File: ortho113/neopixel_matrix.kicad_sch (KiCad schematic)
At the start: 113 parts

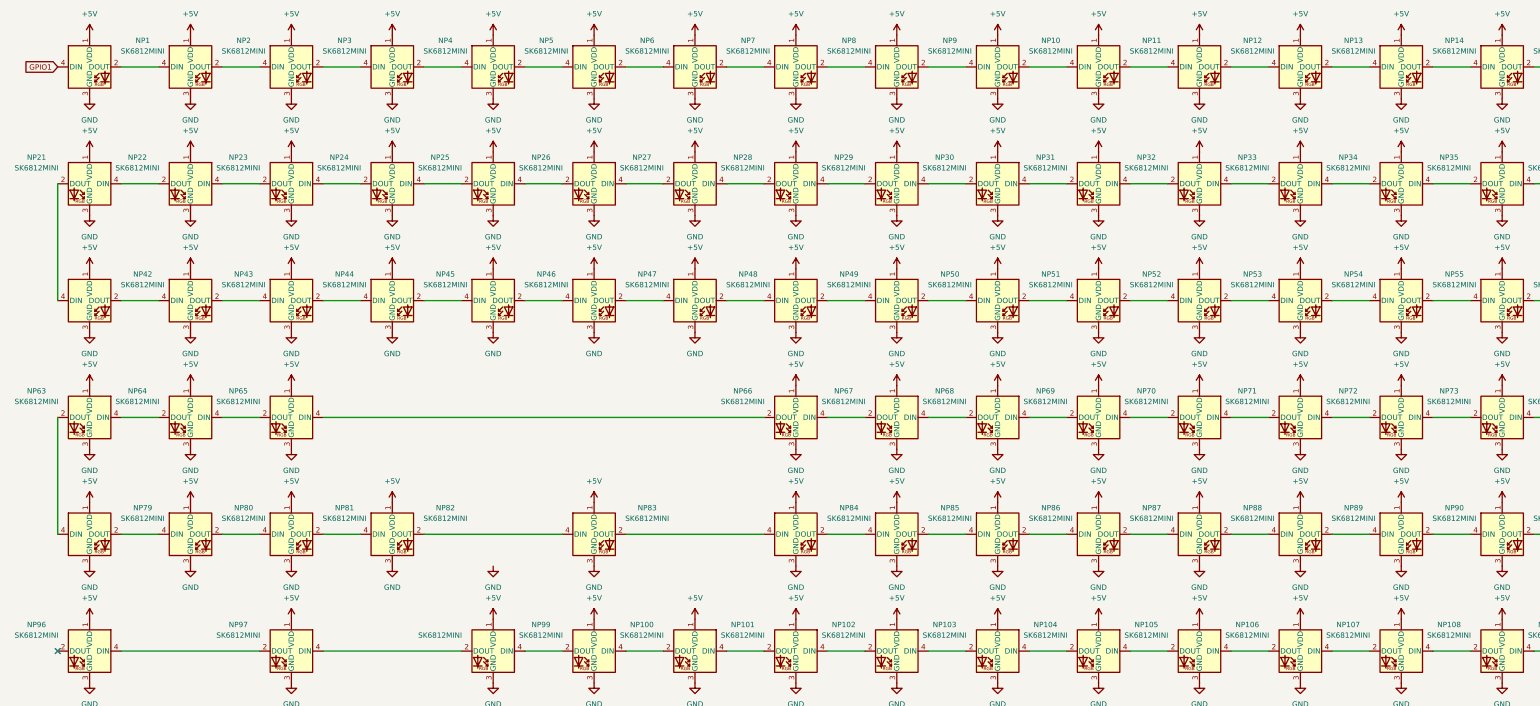
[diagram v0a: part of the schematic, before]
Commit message: fixed submodule conflict & remove gitignore
added pinout for oled display
finished rev1 of pcb design
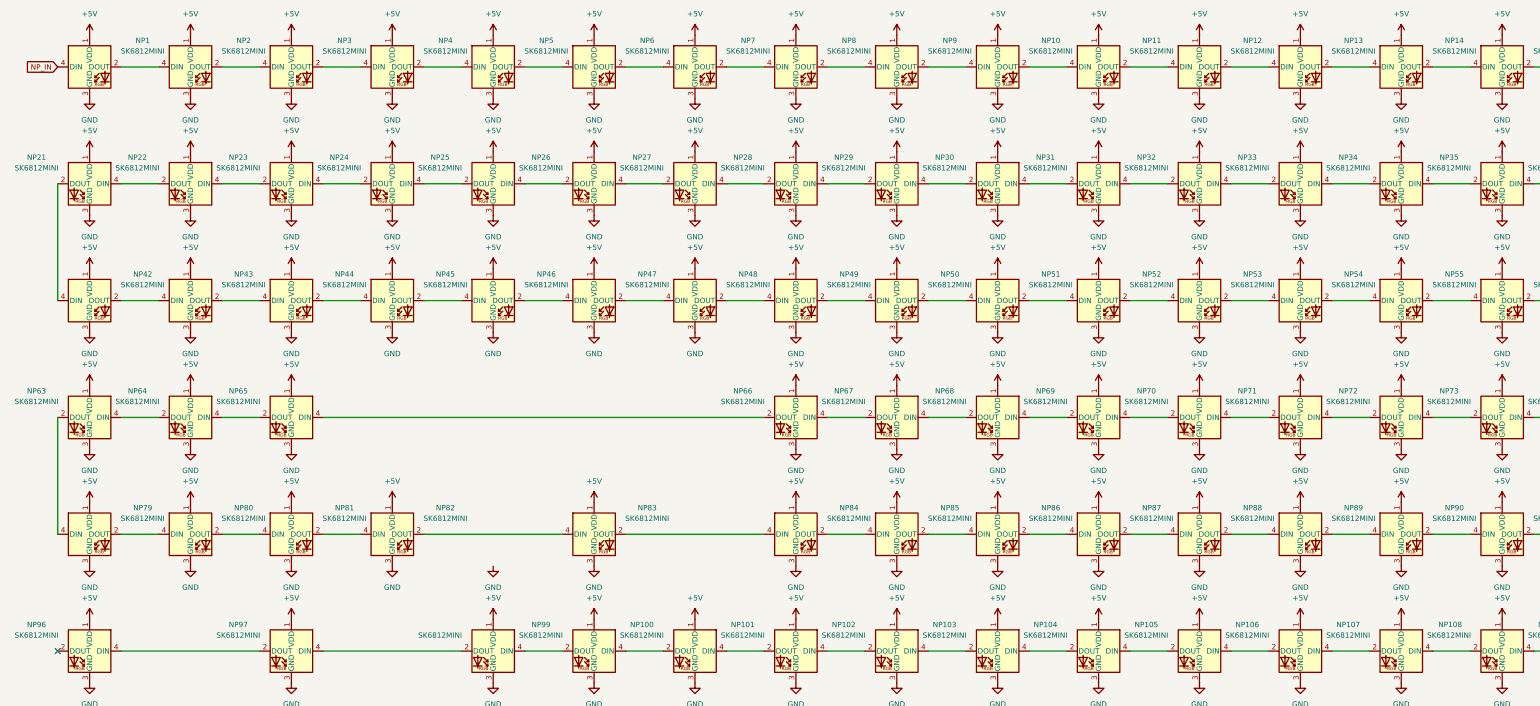
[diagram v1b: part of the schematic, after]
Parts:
- NP1, NP10, NP100, NP101, NP102, NP103, NP104, NP105, NP106, NP107, NP109, NP11, NP110, NP111, NP112, NP113, NP12, NP13, NP14, NP15, NP16, NP17, NP18, NP19, NP2, NP20, NP21, NP22, NP23, NP24, NP25, NP26, NP27, NP28, NP29, NP3, NP30, NP31, NP32, NP33, NP34, NP35, NP36, NP37, NP38, NP39, NP4, NP40, NP41, NP42, NP43, NP44, NP45, NP46, NP47, NP48, NP49, NP5, NP50, NP51, NP52, NP53, NP54, NP55, NP56, NP57, NP58, NP59, NP6, NP60, NP61, NP62, NP63, NP64, NP65, NP66, NP67, NP68, NP69, NP7, NP70, NP71, NP72, NP73, NP74, NP75, NP76, NP77, NP78, NP79, NP8, NP80, NP81, NP82, NP83, NP84, NP85, NP86, NP87, NP88, NP89, NP9, NP90, NP91, NP92, NP93, NP94, NP95, NP96, NP97, NP98, NP99: footprint LED_SMD:LED_SK6812MINI_PLCC4_3.5x3.5mm_P1.75mm -> my-footprints:LED_SK6812MINI_E
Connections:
- net GPIO1 renamed NP_IN

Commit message: forgot to push changes to main
don't remember what happened here
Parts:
- added R3: 500, Resistor_SMD:R_1812_4532Metric_Pad1.30x3.40mm_HandSolder, symbol Device:R_Small
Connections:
- net NP_IN: now also R3.1; no longer NP1.4 (DIN)
- new net: NP1.4 (DIN), R3.2
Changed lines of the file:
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@@
 	(wire
 		(pts
+			(xy 22.86 59.69) (xy 25.4 59.69)
+		)
+		(stroke
+			(width 0)
+			(type default)
+		)
+	)
+	(wire
+		(pts
 			(xy 322.58 199.39) (xy 313.69 199.39)
 		)
@@
 	(wire
 		(pts
+			(xy 30.48 59.69) (xy 33.02 59.69)
+		)
+		(stroke
+			(width 0)
+			(type default)
+		)
+	)
+	(wire
+		(pts
 			(xy 386.08 59.69) (xy 394.97 59.69)
 		)
@@
 	(global_label "NP_IN"
 		(shape input)
-		(at 33.02 59.69 180)
+		(at 22.86 59.69 180)
 		(fields_autoplaced yes)
 		(effects
@@
 		)
 		(property "Intersheetrefs" "${INTERSHEET_REFS}"
-			(at 24.5314 59.69 0)
+			(at 14.3714 59.69 0)
 			(effects
 				(font
@@
 					(unit 1)
 				)
+			)
+		)
+	)
+	(symbol
+		(lib_id "Device:R_Small")
+		(at 27.94 59.69 90)
+		(mirror x)
+		(unit 1)
+		(exclude_from_sim no)
+		(in_bom yes)
+		(on_board yes)
+		(dnp no)
+		(property "Reference" "R3"
+			(at 27.686 59.69 90)
+			(effects
+				(font
+					(size 1.27 1.27)
+				)
+			)
+		)
+		(property "Value" "500"
+			(at 27.94 61.722 90)
+			(effects
+				(font
+					(size 1.27 1.27)
+				)
+			)
+		)
+		(property "Footprint" "Resistor_SMD:R_1812_4532Metric_Pad1.30x3.40mm_HandSolder"
+			(at 27.94 59.69 0)
+			(effects
+				(font
+					(size 1.27 1.27)
+				)
+				(hide yes)
+			)
+		)
+		(property "Datasheet" "~"
+			(at 27.94 59.69 0)
+			(effects
+				(font
+					(size 1.27 1.27)
+				)
+				(hide yes)
+			)
+		)
+		(property "Description" "Resistor, small symbol"
+			(at 27.94 59.69 0)
+			(effects
+				(font
+					(size 1.27 1.27)
+				)
+				(hide yes)
+			)
+		)
+		(pin "1"
+		)
+		(pin "2"
+		)
+		(instances
+			(project "ortho113"
+				(path "/54fa9a7b-8fd8-4dda-b874-5f01b1f0cdfe/5fabd55d-e962-4cb6-8fb4-37116166ba8a"
+					(reference "R3")
+					(unit 1)
+				)
